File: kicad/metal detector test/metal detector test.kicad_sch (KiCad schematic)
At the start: 85 parts, among them J1 SJ-3524-SMT, Q1 2SA2071T100Q, Q2 2SC5824T100Q, SW1 SW_SPST, SW2 SW_SPST, SW3 SW_SPST, SW4 SW_SPST, SW5 SW_SPST, SW6 SW_SPST, SW7 SW_SPST, SW8 SW_SPST, SW9 SW_SPST, U1 LM2940IMP-9.0/NOPB, U10 LT1129CST-3.3#PBF, U11 MAX7423EUA+, U12 OPA2320AID, U2 OPA2140AID, U3 NUCLEO-F303K8, U4 UA78M05CDCYRG3, U5 LT1129CST-3.3#PBF, U6 LM4752TS, U7 MAX7423EUA+, U8 LS20-S, U9 UA78M05CDCYRG3

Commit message: Tweaks to make ERC pass, and redid designator anotations
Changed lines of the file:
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@@
   (junction (at 20.32 73.66) (diameter 0) (color 0 0 0 0)
   )
+  (junction (at 262.89 43.18) (diameter 0) (color 0 0 0 0)
+  )
   (junction (at 30.48 48.26) (diameter 0) (color 0 0 0 0)
   )
@@
     (stroke (width 0) (type default))
   )
-  (wire (pts (xy 260.35 43.18) (xy 265.43 43.18))
+  (wire (pts (xy 260.35 43.18) (xy 262.89 43.18))
     (stroke (width 0) (type default))
   )
@@
     (stroke (width 0) (type default))
   )
+  (wire (pts (xy 262.89 29.21) (xy 262.89 43.18))
+    (stroke (width 0) (type default))
+  )
   (wire (pts (xy 33.02 170.18) (xy 36.83 170.18))
     (stroke (width 0) (type default))
@@
     (stroke (width 0) (type default))
   )
+  (wire (pts (xy 262.89 43.18) (xy 265.43 43.18))
+    (stroke (width 0) (type default))
+  )
   (wire (pts (xy 176.53 69.85) (xy 248.92 69.85))
     (stroke (width 0) (type default))
@@
         )
       )
+    )
+  )
+  (symbol (lib_id "power:PWR_FLAG") (at 262.89 29.21 0) (unit 1)
+    (in_bom yes) (on_board yes) (dnp no) (fields_autoplaced)
+    (property "Reference" "#FLG03" (at 262.89 27.305 0)
+      (effects (font (size 1.27 1.27)) hide)
+    )
+    (property "Value" "PWR_FLAG" (at 262.89 25.4 0)
+      (effects (font (size 1.27 1.27)))
+    )
+    (property "Footprint" "" (at 262.89 29.21 0)
+      (effects (font (size 1.27 1.27)) hide)
+    )
+    (property "Datasheet" "~" (at 262.89 29.21 0)
+      (effects (font (size 1.27 1.27)) hide)
+    )
+    (pin "1")
+    (instances
+      (project "metal detector test"
+        (path "/aac94249-970f-41d5-8c24-6bade512464d"
+          (reference "#FLG03") (unit 1)
+        )
+      )

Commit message: part num for ferrite
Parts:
- FB1: value FerriteBead_Small -> HZ0805E601R-10
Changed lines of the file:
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@@
       (effects (font (size 1.27 1.27)))
     )
-    (property "Value" "FerriteBead_Small" (at 253.9619 40.64 90)
+    (property "Value" "HZ0805E601R-10" (at 253.9619 40.64 90)
       (effects (font (size 1.27 1.27)) hide)
     )

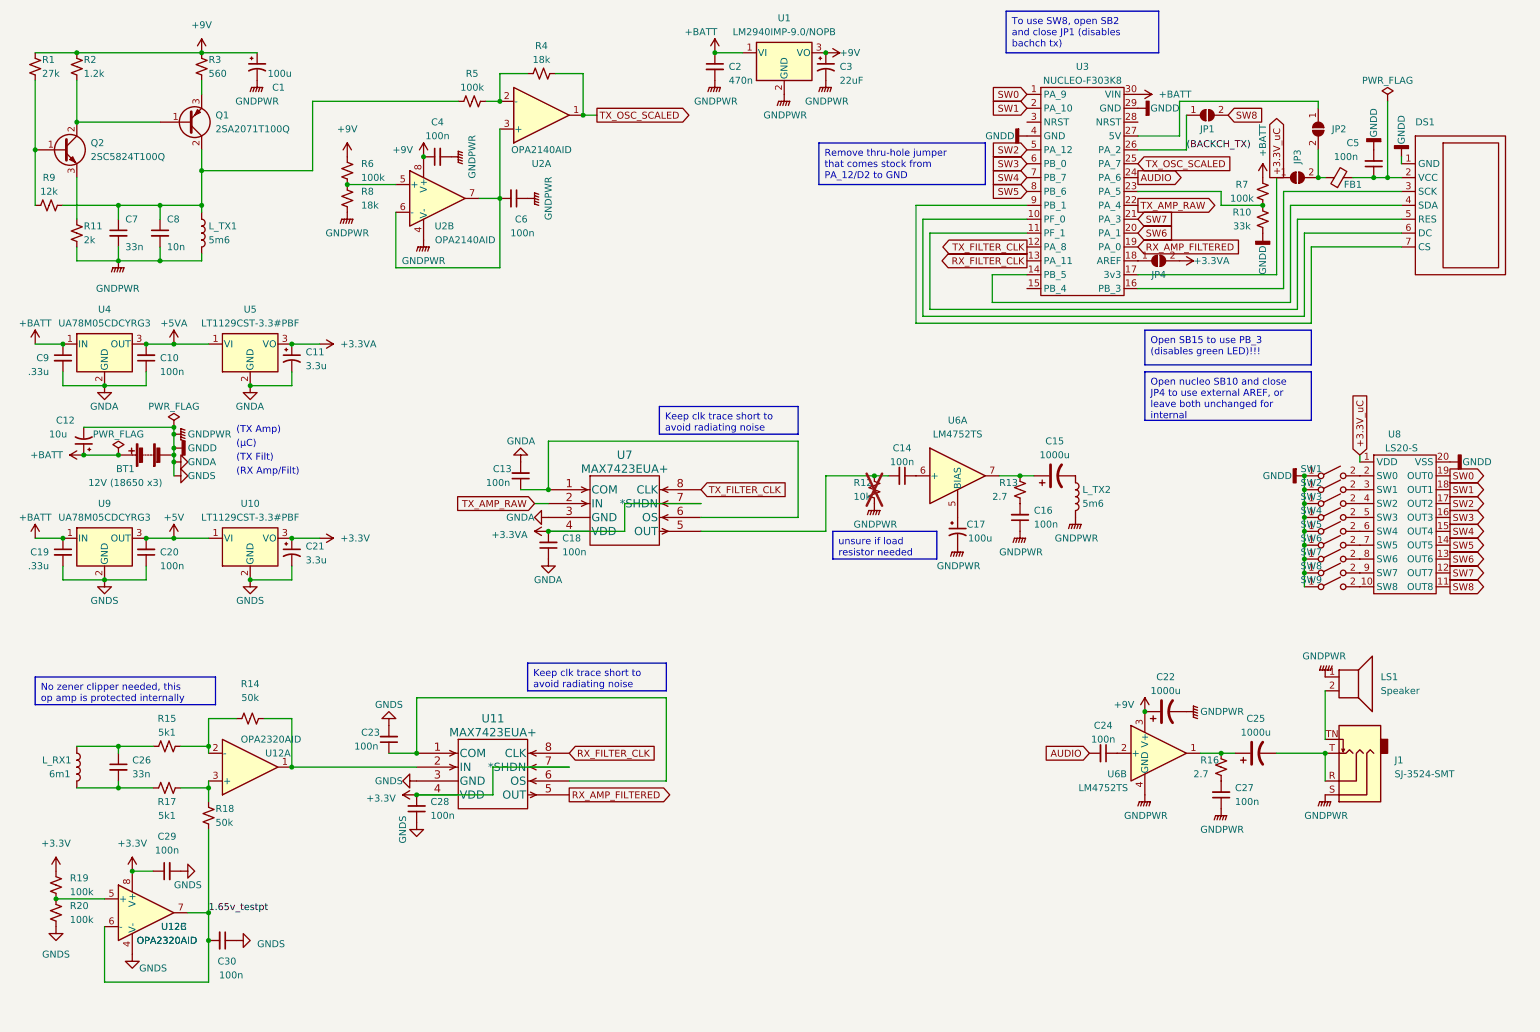
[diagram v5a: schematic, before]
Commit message: Finished adding footprints, made MPN field for manufacturer part number and populated it for each part, figured out push button part and footprint
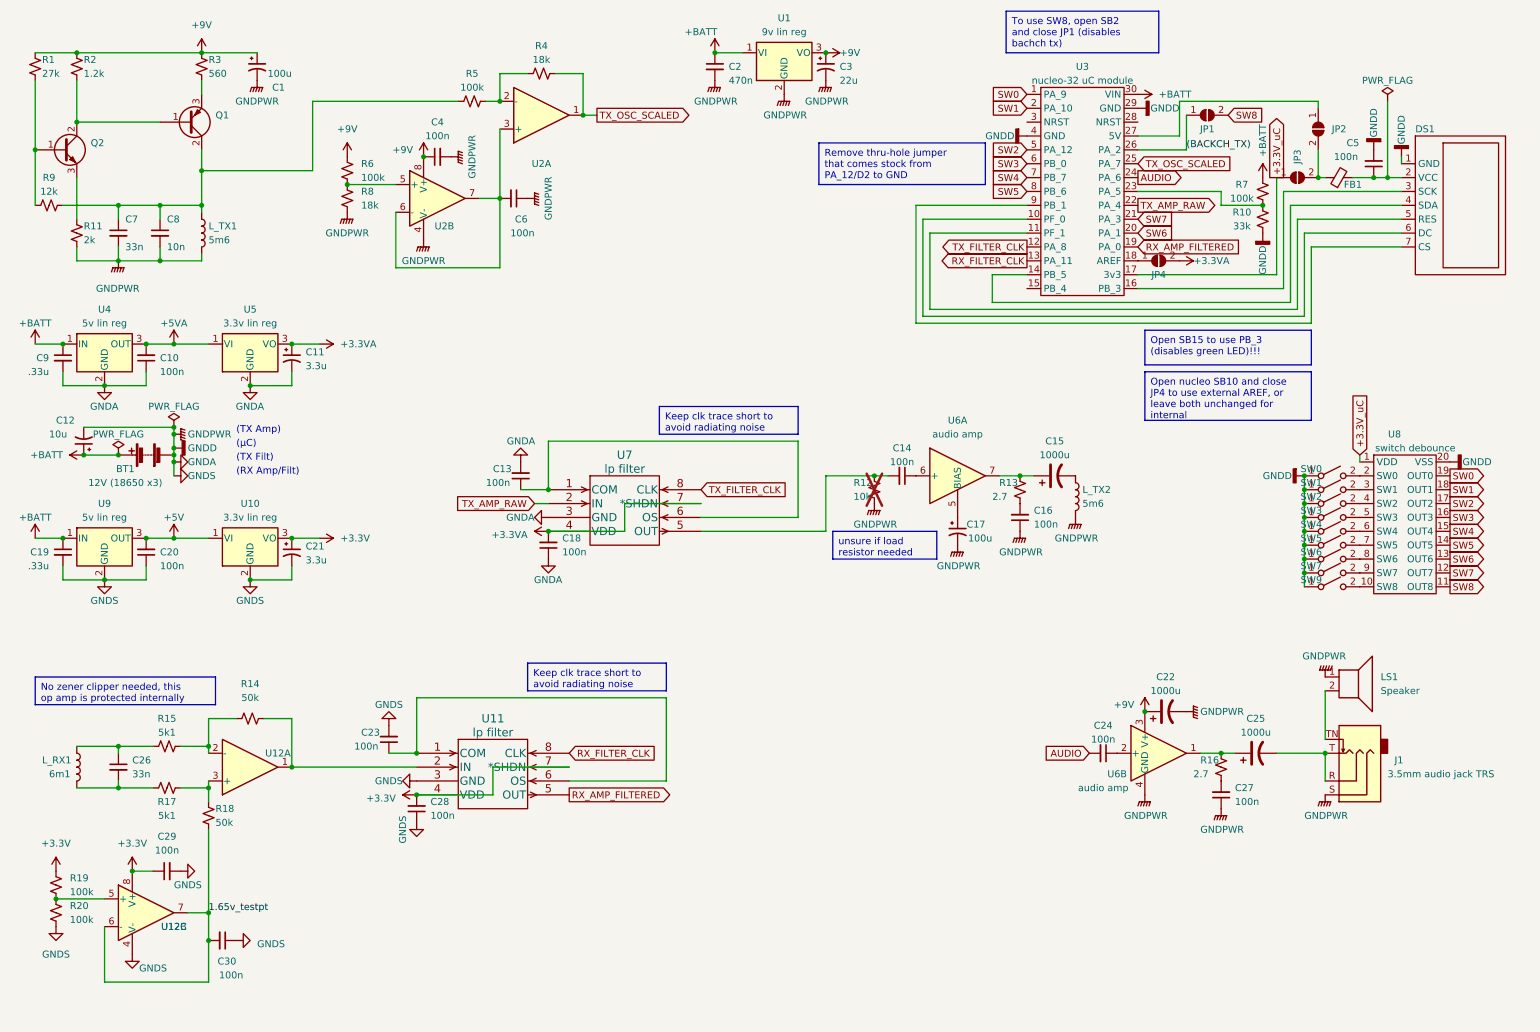
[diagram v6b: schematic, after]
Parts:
- C3: value 22uF -> 22u
- DS1: footprint (none) -> allen footprints:oled_2.42in_128x64; MPN (none) -> ‎B09LND6QJ1
- FB1: value HZ0805E601R-10 -> ~; MPN (none) -> HZ0805E601R-10
- J1: value SJ-3524-SMT -> 3.5mm audio jack TRS; MPN (none) -> SJ-3524-SMT
- Q1: value 2SA2071T100Q -> ~; MPN (none) -> 2SA2071T100Q
- Q2: value 2SC5824T100Q -> ~; MPN (none) -> 2SC5824T100Q
- SW0: renamed from SW1; footprint (none) -> allen footprints:SW_SPST_PTS647; MPN (none) -> PTS 647 SN50 SMTR2 LFS
- SW1: renamed from SW2; footprint (none) -> allen footprints:SW_SPST_PTS647; MPN (none) -> PTS 647 SN50 SMTR2 LFS
- SW2: renamed from SW3; footprint (none) -> allen footprints:SW_SPST_PTS647; MPN (none) -> PTS 647 SN50 SMTR2 LFS
- SW3: renamed from SW4; footprint (none) -> allen footprints:SW_SPST_PTS647; MPN (none) -> PTS 647 SN50 SMTR2 LFS
- SW4: renamed from SW5; footprint (none) -> allen footprints:SW_SPST_PTS647; MPN (none) -> PTS 647 SN50 SMTR2 LFS
- SW5: renamed from SW6; footprint (none) -> allen footprints:SW_SPST_PTS647; MPN (none) -> PTS 647 SN50 SMTR2 LFS
- SW6: renamed from SW7; footprint (none) -> allen footprints:SW_SPST_PTS647; MPN (none) -> PTS 647 SN50 SMTR2 LFS
- SW7: renamed from SW8; footprint (none) -> allen footprints:SW_SPST_PTS647; MPN (none) -> PTS 647 SN50 SMTR2 LFS
- SW9: footprint (none) -> allen footprints:SW_SPST_PTS647; MPN (none) -> PTS 647 SN50 SMTR2 LFS
- U1: value LM2940IMP-9.0/NOPB -> 9v lin reg; MPN (none) -> LM2940IMP-9.0/NOPB
- U10, U5: value LT1129CST-3.3#PBF -> 3.3v lin reg; MPN (none) -> LT1129CST-3.3#PBF
- U11, U7: value MAX7423EUA+ -> lp filter; MPN (none) -> MAX7423EUA+
- U12: value OPA2320AID -> ~; MPN (none) -> OPA2320AID
- U2: value OPA2140AID -> ~; MPN (none) -> OPA2140AID
- U3: value NUCLEO-F303K8 -> nucleo-32 uC module; footprint (none) -> allen footprints:Nucleo-32_allen; MPN (none) -> NUCLEO-F303K8
- U4, U9: value UA78M05CDCYRG3 -> 5v lin reg; MPN (none) -> UA78M05CDCYRG3
- U6: value LM4752TS -> audio amp; MPN (none) -> LM4752TS
- U8: value LS20-S -> switch debounce; MPN (none) -> LS20-S

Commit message: Starting PCB layout.  Also added alternate MPNs for a few more regulators sampled from TI
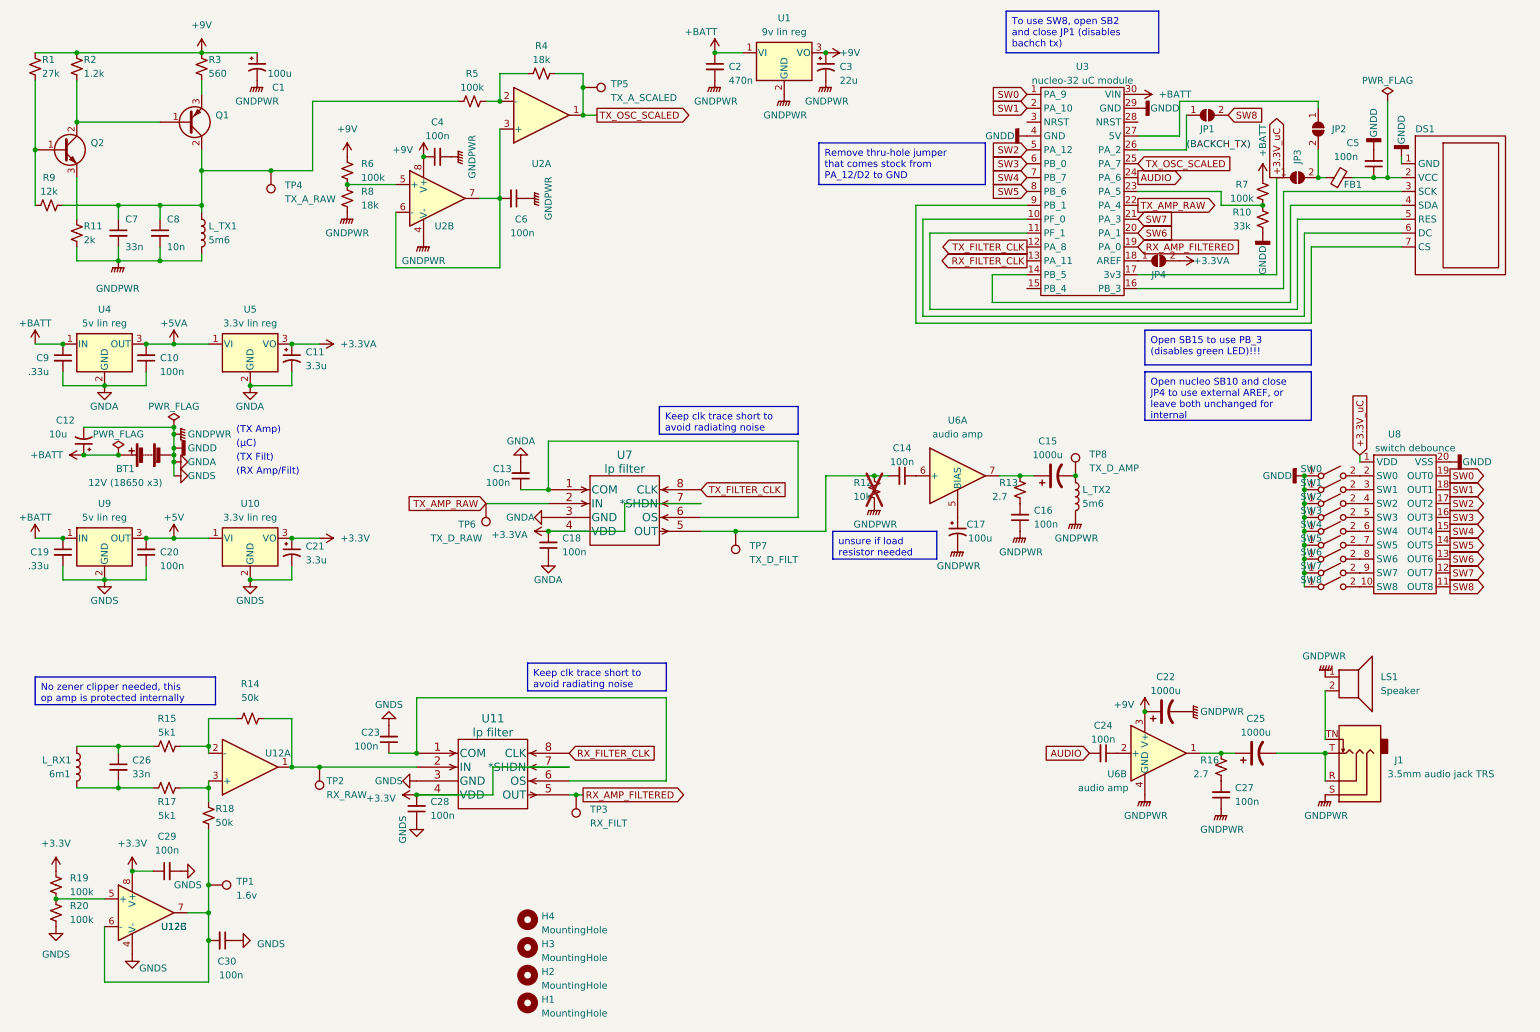
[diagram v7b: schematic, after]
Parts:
- added H1, H2, H3, H4: MountingHole, MountingHole:MountingHole_3.7mm, symbol Mechanical:MountingHole
- added TP1: 1.6v, TestPoint:TestPoint_Pad_D1.5mm, symbol Connector:TestPoint
- added TP2: RX_RAW, TestPoint:TestPoint_Pad_D1.5mm, symbol Connector:TestPoint
- added TP3: RX_FILT, TestPoint:TestPoint_Pad_D1.5mm, symbol Connector:TestPoint
- added TP4: TX_A_RAW, TestPoint:TestPoint_Pad_D1.5mm, symbol Connector:TestPoint
- added TP5: TX_A_SCALED, TestPoint:TestPoint_Pad_D1.5mm, symbol Connector:TestPoint
- added TP6: TX_D_RAW, TestPoint:TestPoint_Pad_D1.5mm, symbol Connector:TestPoint
- added TP7: TX_D_FILT, TestPoint:TestPoint_Pad_D1.5mm, symbol Connector:TestPoint
- added TP8: TX_D_AMP, TestPoint:TestPoint_Pad_D1.5mm, symbol Connector:TestPoint
- U10, U5: Alt MPN (none) -> UA78M33QDCYRG4Q1
- U4, U9: Alt MPN (none) -> LM2940IMP-5.0/NOPB
- renumbered SW9 to SW8
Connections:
- net RX_AMP_FILTERED: now also TP3.1
- net TX_AMP_RAW: now also TP6.1
- net TX_OSC_SCALED: now also TP5.1
- net at R14.2, U11.2 (IN), U12.1: now also TP2.1
- net at C14.2, R12.1, U7.5 (OUT): now also TP7.1
- net at C7.1, C8.1, L_TX1.1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: now also TP4.1
- net at C15.2, L_TX2.1: now also TP8.1
- net 1.65v_testpt: no longer names the net of C30.2, R18.2, U12.6 (-), U12.7
- net 1.65v_testpt: now also TP1.1
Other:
- title: (none) -> Lumber Plunder Metal Detector

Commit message: Working on pcb layout, generated BOM
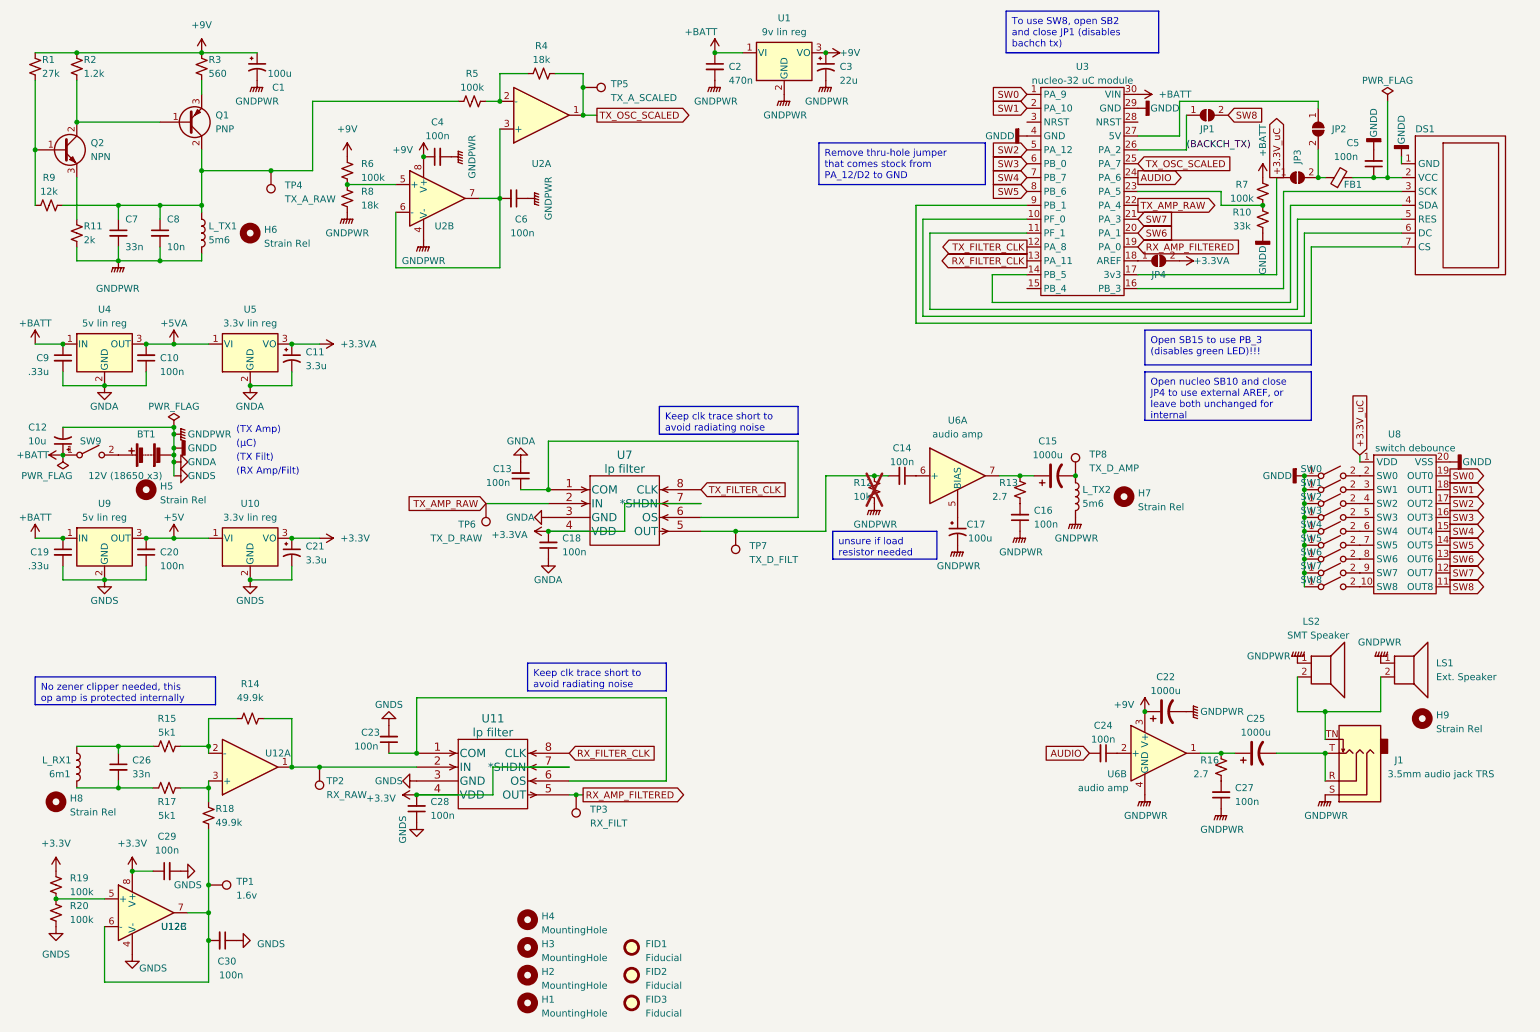
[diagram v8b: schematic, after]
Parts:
- added FID1, FID2, FID3: Fiducial, Fiducial:Fiducial_0.5mm_Mask1.5mm, symbol Mechanical:Fiducial
- added H5, H6, H7, H8, H9: Strain Rel, MountingHole:MountingHole_3.2mm_M3, symbol Mechanical:MountingHole
- added LS2: SMT Speaker, allen footprints:CDS-13138-SMT-TR_speaker_smt, symbol Device:Speaker
- added SW9: SW_SPST, allen footprints:A11AH_right_angle_toggle_switch, symbol Switch:SW_SPST
- BT1: MPN (none) -> 106990288
- C1, C12, C17, C3: footprint Capacitor_SMD:C_1206_3216Metric_Pad1.33x1.80mm_HandSolder -> allen footprints:C_Polarized_1206_3216Metric_HandSolder_allen
- C11, C21: footprint Capacitor_SMD:C_0805_2012Metric_Pad1.18x1.45mm_HandSolder -> allen footprints:C_Polarized_0805_2012Metric_HandSolder_allen
- C15, C22, C25: MPN (none) -> A750MV108M1EAAE014
- DS1: MPN ‎B09LND6QJ1 -> B09LND6QJ1
- FB1: value ~ -> ferrite bead smt
- LS1: value Speaker -> Ext. Speaker
- Q1: value ~ -> PNP
- Q2: value ~ -> NPN
- R14, R18: value 50k -> 49.9k
- U12: value ~ -> op amp (lower voltage)
- U2: value ~ -> op amp (higher voltage)
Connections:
- net +BATT: now also SW9.1 (A); no longer BT1.1 (+)
- net GNDA: now also LS2.1
- net at J1.TN, LS1.2: now also LS2.2
- new net: BT1.1 (+), SW9.2 (B)
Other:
- moved on the sheet: C12, LS1
